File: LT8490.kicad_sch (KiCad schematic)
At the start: 120 parts, among them J1 Conn_01x01, J10 Conn_01x01, J11 Conn_01x01, J12 Conn_01x01, J13 Conn_01x01, J14 Conn_01x01, J15 Conn_01x01, J16 Conn_01x01, J17 Conn_01x01, J18 Conn_01x01, J19 Conn_01x01, J2 Conn_01x01, J20 Conn_01x01, J21 Conn_01x01, J22 Conn_01x01, J23 Conn_01x01, J24 Conn_01x01, J25 Conn_01x01, J3 Conn_01x01, J4 Conn_01x01, J5 Conn_01x01, J6 Conn_01x01, J7 Conn_01x01, J8 Conn_01x01, J9 Conn_01x01, Q1 Si7106DN, Q2 Si7106DN, Q3 Si7106DN, Q4 Si7106DN, Q5 BSS84, Q6 MBT2222ADW1T1, U4 LT8490EUKJPBF

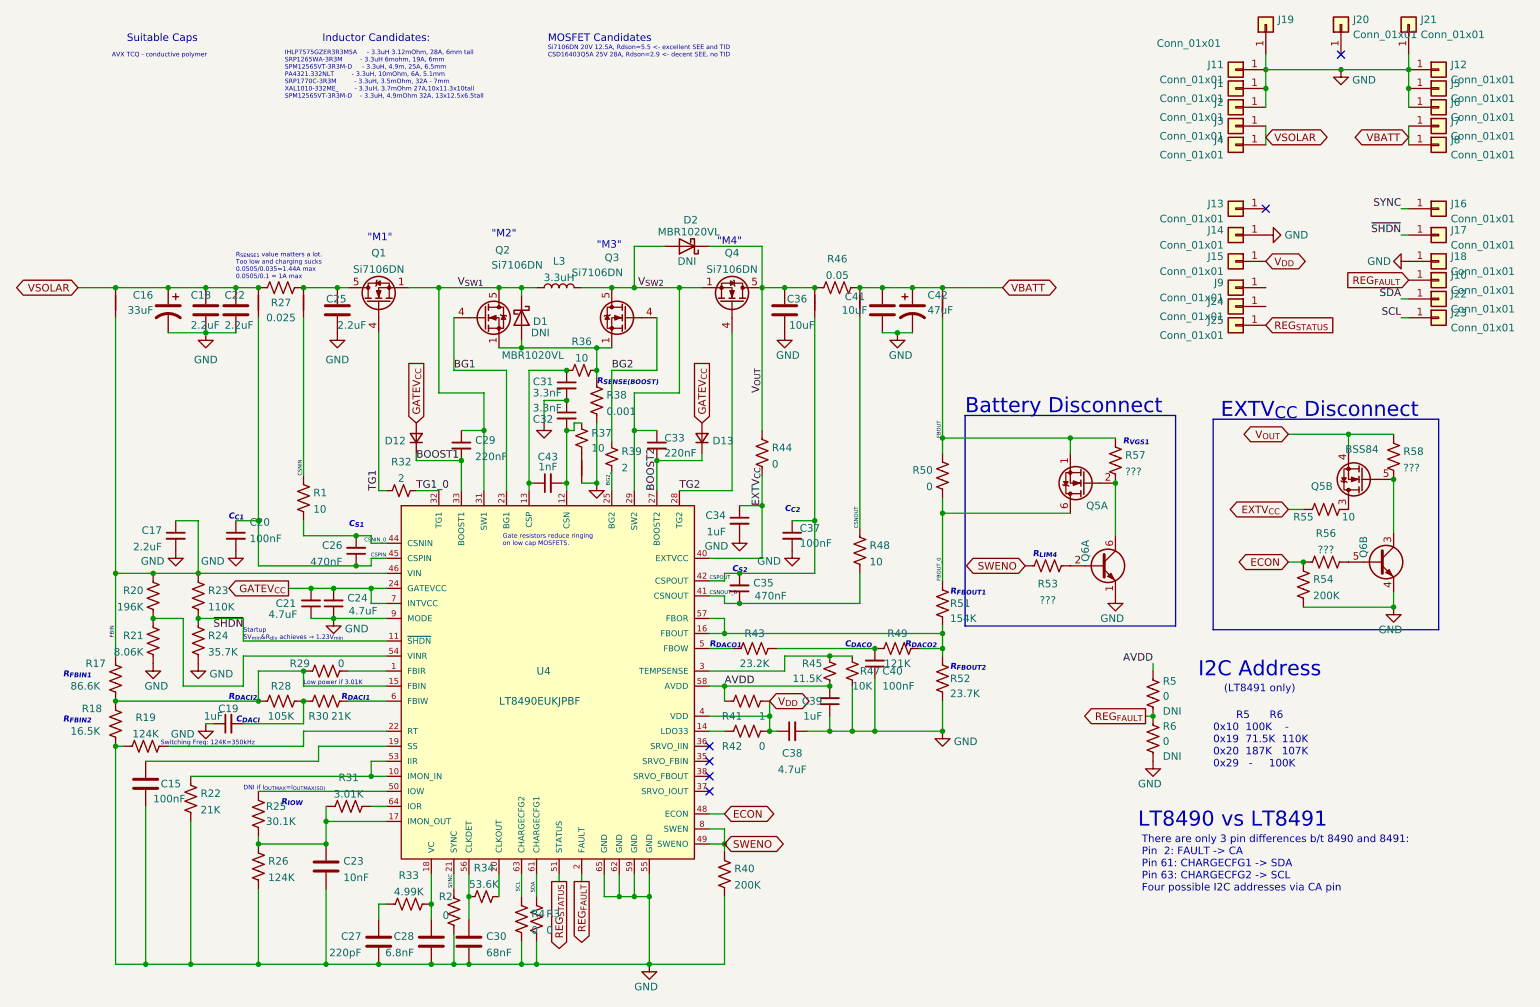
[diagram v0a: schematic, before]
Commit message: tweaks after v00 build
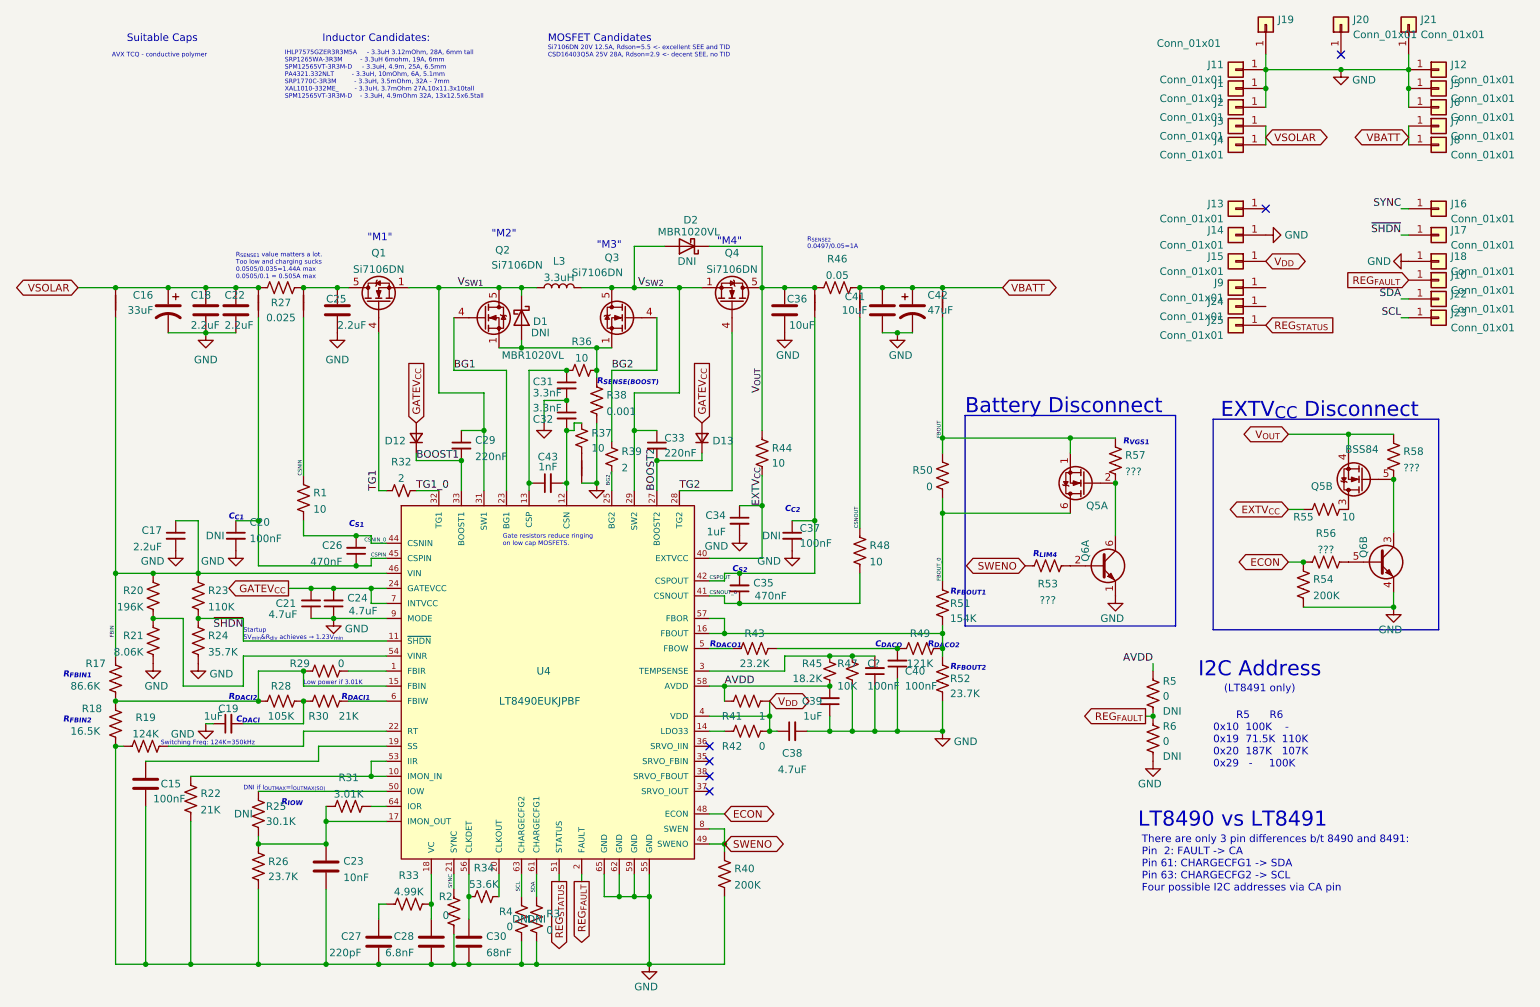
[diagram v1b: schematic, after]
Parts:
- added C?: 100nF, Capacitor_SMD:C_0603_1608Metric, symbol Device:C_Small
- R26: value 124K -> 23.7K
- R3, R4: DNI (none) -> DNI
- R44: value 0 -> 10
- R45: value 11.5K -> 18.2K
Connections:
- net GND: now also C?.1
- net at R45.1, R47.2, U4.3 (TEMPSENSE): now also C?.2
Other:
- note added: "R_{SENSE1} value matters a lot. Too low and charging sucks 0.0505/0.035=1.44A max 0.0505/0.1 = 0.505A max"
- note added: "R_{SENSE2} 0.0497/0.05=1A"
- note removed: "R_{SENSE1} value matters a lot. Too low and charging sucks 0.0505/0.035=1.44A max 0.0505/0.1 = 1A max"
- moved on the sheet: C40, R49

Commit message: tweaking performance
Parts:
- added R?: 4, Resistor_SMD:R_0603_1608Metric, symbol Device:R_Small_US
- C20, C37: value 100nF -> 10nF; DNI DNI -> (none)
- D1, D2: DNI DNI -> (none)
- R2: value 0 -> 10K
- R27: value 0.025 -> 0.1
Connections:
- net GATEV_{CC}: now also R?.2; no longer D12.2 (A), D13.2 (A)
- net GND: now also D1.2 (A), D2.2 (A)
- net V_{OUT}: no longer D2.1 (K)
- net V_{SW2}: now also D2.1 (K); no longer D2.2 (A)
- net RS+: now reaches Q2.1 (S), Q2.2 (S), Q2.3 (S), Q3.1 (S), Q3.2 (S), Q3.3 (S), R36.1, R38.1
- net RS+: no longer D1.2 (A)
- new net GATEV_{CC}`: D12.2 (A), D13.2 (A), R?.1
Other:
- moved on the sheet: D1, D2

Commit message: minor tweaks after bench testing
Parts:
- R54: DNI DNi -> DNI; now left out of the parts list
- R55: now left out of the parts list
- gave numbers to parts that had none: 2
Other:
- note added: "R_{IMON_IN}"
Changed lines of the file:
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@@
     (effects (font (size 2.54 2.54)) (justify left bottom))
   )
+  (text "R_{IMON_IN}" (at 58.42 143.51 0)
+    (effects (font (size 1.016 1.016) (thickness 0.254) bold italic) (justify left bottom))
+  )
   (text "Startup\n5V_{min}&R_{div} achieves → 1.23V_{min}" (at 66.04 120.65 0)
     (effects (font (size 0.762 0.762)) (justify left bottom))
@@
     (effects (font (size 1.27 1.27)) (justify left bottom))
   )
-  (text "\"M3\"" (at 125.73 54.61 0)
+  (text "\"M3\"" (at 124.46 54.61 0)
     (effects (font (size 1.27 1.27)) (justify left bottom))
   )
@@
     (effects (font (size 1.016 1.016) (thickness 0.254) bold italic) (justify left bottom))
   )
-  (text "R_{IOW}" (at 72.39 148.59 0)
+  (text "R_{IOW}" (at 64.77 148.59 0)
     (effects (font (size 1.016 1.016) (thickness 0.254) bold italic) (justify left bottom))
   )
@@
   (symbol (lib_id "Device:R_US") (at 201.93 107.95 90) (unit 1)
     (in_bom yes) (on_board yes) (fields_autoplaced)
-    (property "Reference" "R53" (id 0) (at 201.93 110.9885 90))
-    (property "Value" "???" (id 1) (at 201.93 113.7636 90))
+    (property "Reference" "R53" (id 0) (at 201.93 110.8694 90))
+    (property "Value" "???" (id 1) (at 201.93 113.4063 90))
     (property "Footprint" "Resistor_SMD:R_0603_1608Metric" (id 2) (at 202.184 106.934 90)
       (effects (font (size 1.27 1.27)) hide)
@@
       (effects (font (size 1.27 1.27)) hide)
     )
-    (property "DNI" "DNI" (id 4) (at 201.93 107.95 90)
-      (effects (font (size 1.27 1.27)) hide)
-    )
+    (property "DNI" "DNI" (id 4) (at 201.93 115.9432 90))
     (property "Description" "??? 0603" (id 5) (at 201.93 123.6885 90)
       (effects (font (size 1.27 1.27)) hide)
@@
   (symbol (lib_id "Transistor_FET:Si7336ADP") (at 130.81 66.04 0) (mirror y) (unit 1)
     (in_bom yes) (on_board yes)
-    (property "Reference" "Q3" (id 0) (at 129.54 55.88 0)
+    (property "Reference" "Q3" (id 0) (at 128.27 55.88 0)
       (effects (font (size 1.27 1.27)) (justify left))
     )
-    (property "Value" "Si7106DN" (id 1) (at 130.175 58.42 0)
+    (property "Value" "Si7106DN" (id 1) (at 132.08 58.42 0)
       (effects (font (size 1.27 1.27)) (justify left))
     )
@@
   (symbol (lib_id "Device:L") (at 119.38 60.96 90) (unit 1)
     (in_bom yes) (on_board yes)
-    (property "Reference" "L3" (id 0) (at 119.38 56.4855 90))
-    (property "Value" "3.3uH" (id 1) (at 119.38 59.2606 90))
+    (property "Reference" "L3" (id 0) (at 119.38 58.42 90))
+    (property "Value" "3.3uH" (id 1) (at 119.38 62.23 90))
     (property "Footprint" "custom-footprints:L_SRP1770C" (id 2) (at 119.38 60.96 0)
       (effects (font (size 1.27 1.27)) hide)
@@
   )
   (symbol (lib_id "Device:R_US") (at 248.92 98.425 270) (unit 1)
-    (in_bom yes) (on_board yes)
+    (in_bom no) (on_board yes)
     (property "Reference" "R55" (id 0) (at 245.11 99.695 90))
     (property "Value" "10" (id 1) (at 252.73 99.695 90))
@@
       (effects (font (size 1.27 1.27)) hide)
     )
-    (property "DNI" "DNI" (id 4) (at 248.92 98.425 90)
-      (effects (font (size 1.27 1.27)) hide)
-    )
+    (property "DNI" "DNI" (id 4) (at 248.92 96.52 90))
     (property "Description" "10 0603" (id 5) (at 245.11 112.395 90)
       (effects (font (size 1.27 1.27)) hide)
@@
   (symbol (lib_id "power:GND") (at 219.71 140.97 0) (unit 1)
     (in_bom yes) (on_board yes)
-    (property "Reference" "#PWR?" (id 0) (at 219.71 147.32 0)
+    (property "Reference" "#PWR0106" (id 0) (at 219.71 147.32 0)
       (effects (font (size 1.27 1.27)) hide)
     )
@@
   (symbol (lib_id "Device:R_Small_US") (at 74.93 114.3 180) (unit 1)
     (in_bom yes) (on_board yes) (fields_autoplaced)
-    (property "Reference" "R?" (id 0) (at 76.581 113.4653 0)
+    (property "Reference" "R7" (id 0) (at 76.581 113.4653 0)
       (effects (font (size 1.27 1.27)) (justify right))
     )
@@
   (symbol (lib_id "ypanel-rescue:BSS138DWQ-7-symbols") (at 254 93.345 180) (unit 2)
     (in_bom yes) (on_board yes)
-    (property "Reference" "Q5" (id 0) (at 250.063 94.5134 0)
+    (property "Reference" "Q5" (id 0) (at 250.19 90.17 0)
       (effects (font (size 1.27 1.27)) (justify left))
     )
@@
   (symbol (lib_id "power:GND") (at 132.08 46.99 180) (unit 1)
     (in_bom yes) (on_board yes)
-    (property "Reference" "#PWR?" (id 0) (at 132.08 40.64 0)
+    (property "Reference" "#PWR0105" (id 0) (at 132.08 40.64 0)
       (effects (font (size 1.27 1.27)) hide)
     )
@@
   (symbol (lib_id "Transistor_BJT:MBT2222ADW1T1") (at 210.82 107.95 0) (unit 1)
     (in_bom yes) (on_board yes)
-    (property "Reference" "Q6" (id 0) (at 208.28 105.41 90))
+    (property "Reference" "Q6" (id 0) (at 210.82 104.14 0))
     (property "Value" "MBT2222ADW1T1" (id 1) (at 215.6714 109.093 0)
       (effects (font (size 1.27 1.27)) (justify left) hide)
@@
   )
   (symbol (lib_id "Device:R_US") (at 245.11 111.125 0) (unit 1)
-    (in_bom yes) (on_board yes) (fields_autoplaced)
-    (property "Reference" "R54" (id 0) (at 246.761 110.2165 0)
+    (in_bom no) (on_board yes) (fields_autoplaced)
+    (property "Reference" "R54" (id 0) (at 246.761 109.0219 0)
       (effects (font (size 1.27 1.27)) (justify left))
     )
-    (property "Value" "200K" (id 1) (at 246.761 112.9916 0)
+    (property "Value" "200K" (id 1) (at 246.761 111.5588 0)
       (effects (font (size 1.27 1.27)) (justify left))
     )
@@
       (effects (font (size 1.27 1.27)) hide)
     )
-    (property "DNI" "DNi" (id 4) (at 245.11 111.125 0)
-      (effects (font (size 1.27 1.27)) hide)
+    (property "DNI" "DNI" (id 4) (at 246.761 114.0957 0)
+      (effects (font (size 1.27 1.27)) (justify left))
     )
     (property "Description" "200K 0603" (id 5) (at 246.761 122.9165 0)
@@
   (symbol (lib_id "Device:C_Small") (at 172.72 125.73 180) (unit 1)
     (in_bom yes) (on_board yes)
-    (property "Reference" "C?" (id 0) (at 171.45 124.46 0)
+    (property "Reference" "C1" (id 0) (at 171.45 124.46 0)
       (effects (font (size 1.27 1.27)) (justify right))
     )
@@
   (symbol (lib_id "Transistor_BJT:MBT2222ADW1T1") (at 257.81 107.315 0) (unit 2)
     (in_bom yes) (on_board yes)
-    (property "Reference" "Q6" (id 0) (at 255.27 104.775 90))
+    (property "Reference" "Q6" (id 0) (at 257.81 102.87 0))
     (property "Value" "MBT2222ADW1T1" (id 1) (at 238.76 107.315 90)
       (effects (font (size 1.27 1.27)) hide)
@@
   (symbol (lib_id "power:GND") (at 113.03 46.99 180) (unit 1)
     (in_bom yes) (on_board yes)
-    (property "Reference" "#PWR?" (id 0) (at 113.03 40.64 0)
+    (property "Reference" "#PWR0104" (id 0) (at 113.03 40.64 0)
       (effects (font (size 1.27 1.27)) hide)
     )
@@
       (reference "#PWR0103") (unit 1) (value "GND") (footprint "")
     )
+    (path "/f5b96039-a604-4859-8da1-3c4a5b965043"
+      (reference "#PWR0104") (unit 1) (value "GND") (footprint "")
+    )
+    (path "/9fb38c5f-237a-449e-b9d2-0636a5415724"
+      (reference "#PWR0105") (unit 1) (value "GND") (footprint "")
+    )
+    (path "/7373b6a4-abf0-408b-bb8f-eef8e15a1fa6"
+      (reference "#PWR0106") (unit 1) (value "GND") (footprint "")
+    )
     (path "/caec4bf3-07fc-48d4-88f5-bc60f6b9a55e"
       (reference "#PWR0111") (unit 1) (value "GND") (footprint "")
@@
       (reference "#PWR0128") (unit 1) (value "GND") (footprint "")
     )
-    (path "/7373b6a4-abf0-408b-bb8f-eef8e15a1fa6"
-      (reference "#PWR?") (unit 1) (value "GND") (footprint "")
-    )
-    (path "/9fb38c5f-237a-449e-b9d2-0636a5415724"
-      (reference "#PWR?") (unit 1) (value "GND") (footprint "")
-    )
-    (path "/f5b96039-a604-4859-8da1-3c4a5b965043"
-      (reference "#PWR?") (unit 1) (value "GND") (footprint "")
+    (path "/c9dd3c46-fd36-4980-8dd8-b4622adedb48"
+      (reference "C1") (unit 1) (value "100nF") (footprint "Capacitor_SMD:C_0603_1608Metric")
     )
     (path "/acb1e74d-a19c-4f23-b04a-efc44089f9fa"
@@
       (reference "C43") (unit 1) (value "1nF") (footprint "Capacitor_SMD:C_0603_1608Metric")
     )
-    (path "/c9dd3c46-fd36-4980-8dd8-b4622adedb48"
-      (reference "C?") (unit 1) (value "100nF") (footprint "Capacitor_SMD:C_0603_1608Metric")
-    )
     (path "/735821d5-c933-409c-b96d-1d60d9085727"
       (reference "D1") (unit 1) (value "MBR1020VL") (footprint "Diode_SMD:D_SOD-123F")
@@
       (reference "R6") (unit 1) (value "0") (footprint "Resistor_SMD:R_0402_1005Metric")
     )
+    (path "/7968e238-3675-4fd0-aab1-6058157e7a58"
+      (reference "R7") (unit 1) (value "4") (footprint "Resistor_SMD:R_0603_1608Metric")
+    )
     (path "/8c9b241c-1d18-4f70-8eb0-c75268d36f6f"
       (reference "R17") (unit 1) (value "86.6K") (footprint "Resistor_SMD:R_0603_1608Metric")
@@
       (reference "R58") (unit 1) (value "???") (footprint "Resistor_SMD:R_0603_1608Metric")
     )
-    (path "/7968e238-3675-4fd0-aab1-6058157e7a58"
-      (reference "R?") (unit 1) (value "4") (footprint "Resistor_SMD:R_0603_1608Metric")
-    )
     (path "/3cf8d523-f75d-44a2-a167-b24835b4cba3"
